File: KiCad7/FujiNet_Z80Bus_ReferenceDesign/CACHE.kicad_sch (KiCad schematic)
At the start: 4 parts, among them IC2 74590N, IC3 74590N

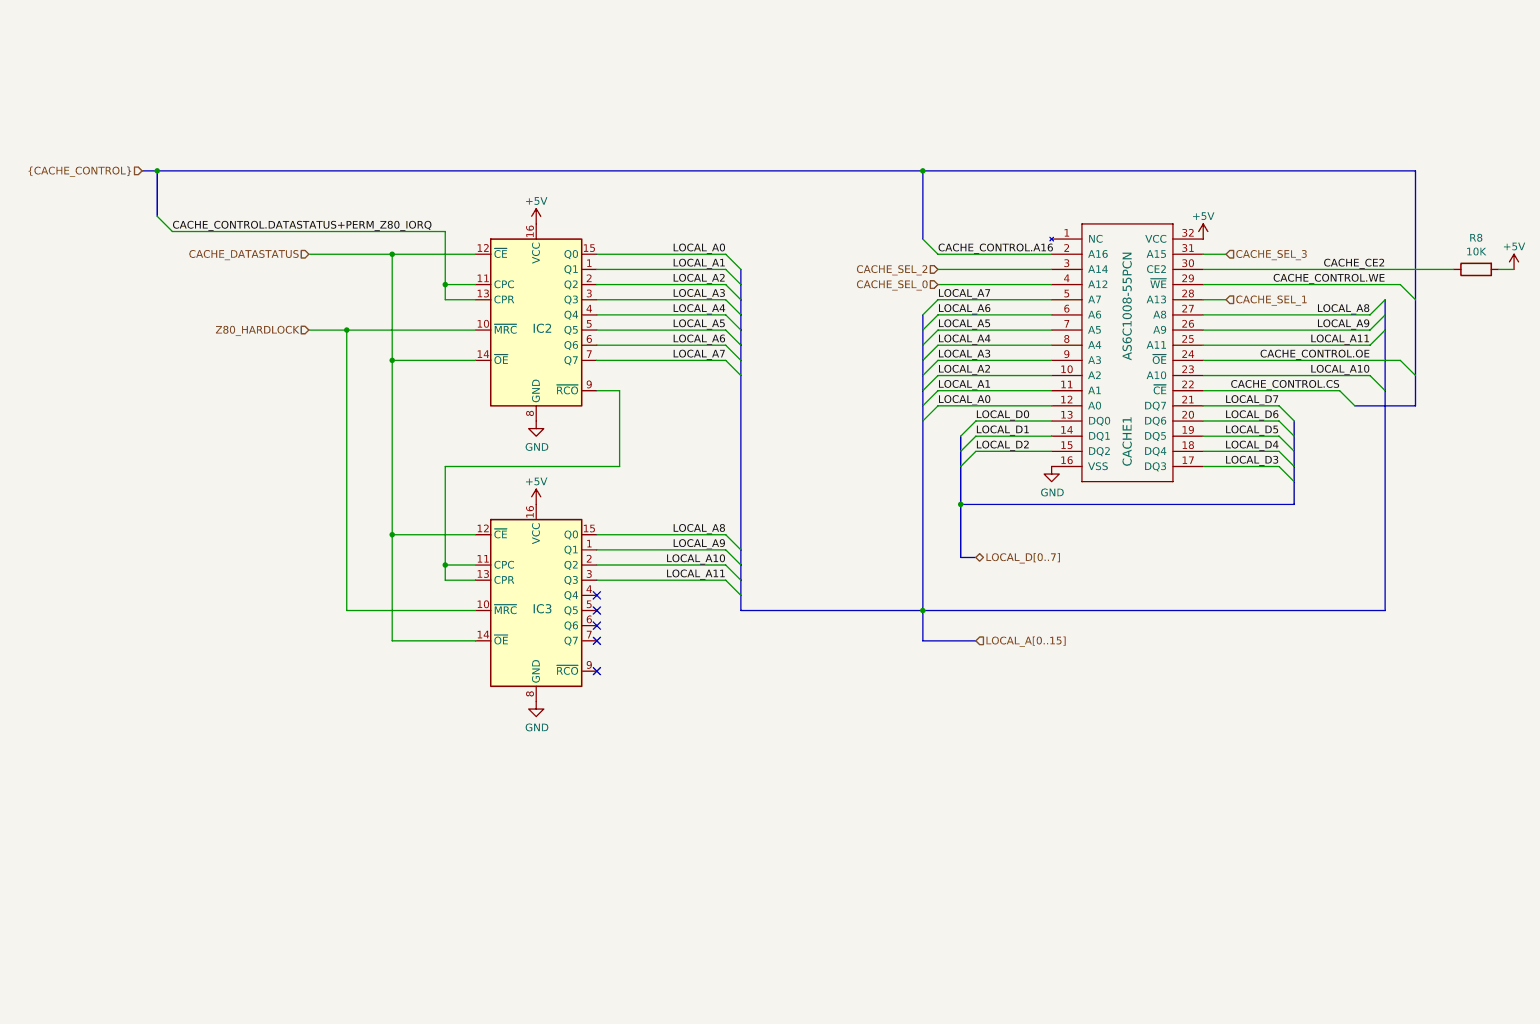
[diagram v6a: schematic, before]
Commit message: KiCad - Swapped out RIO and CACHE symbols
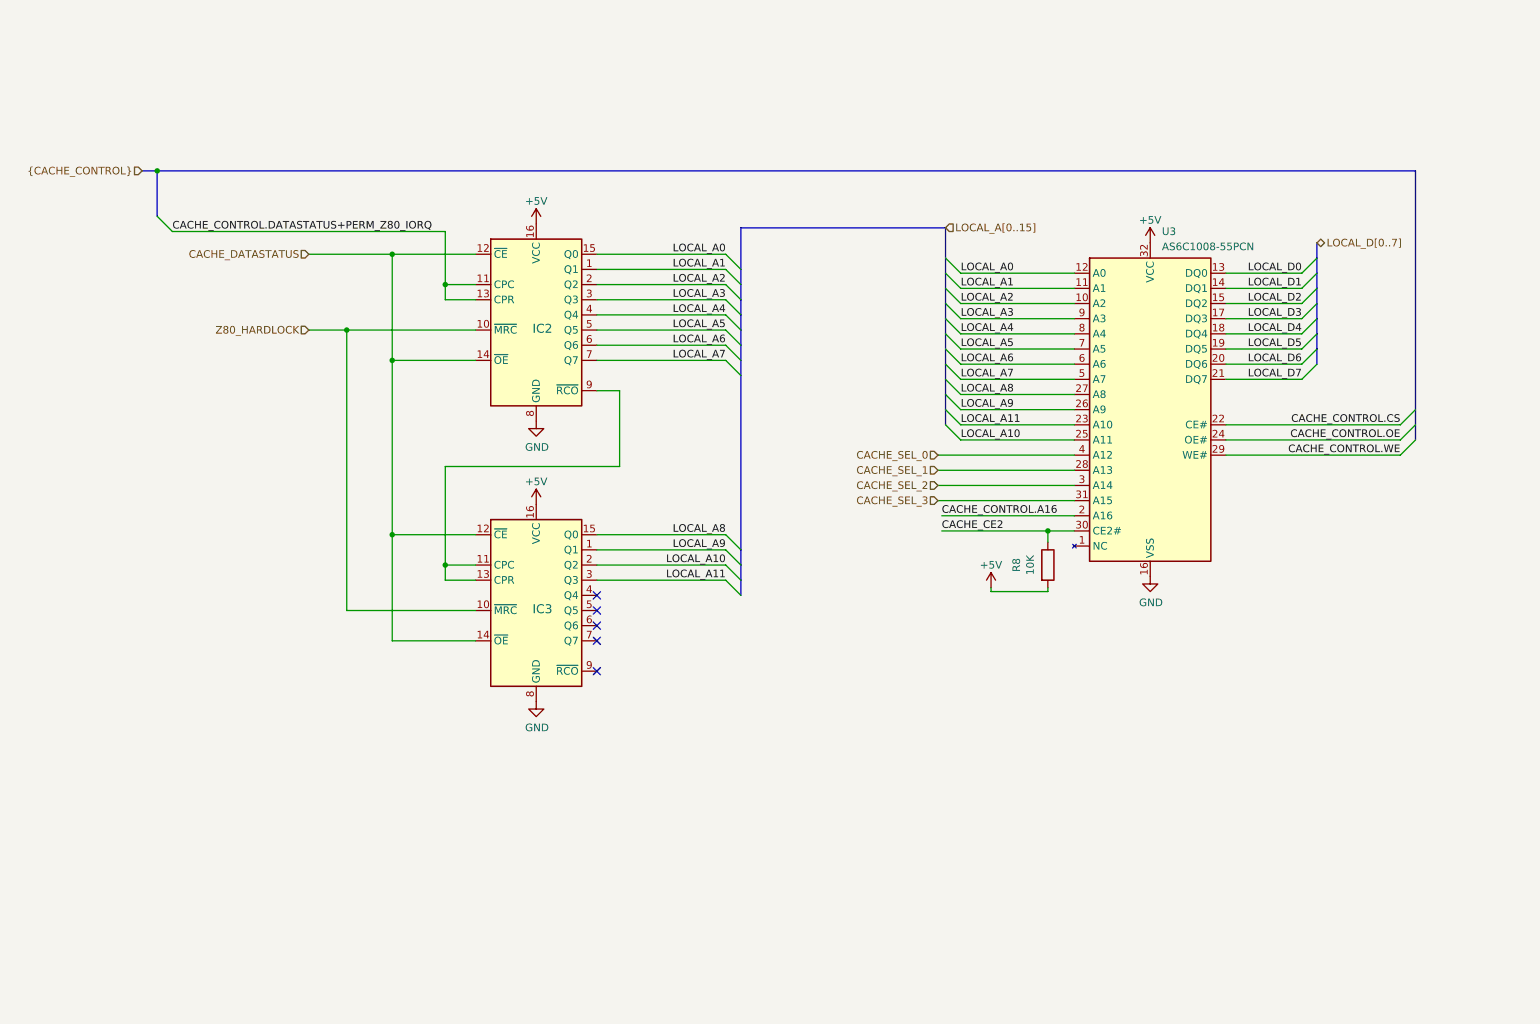
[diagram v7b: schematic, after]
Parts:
- removed CACHE1: AS6C1008-55PCN, Package_DIP:DIP-32_W15.24mm_Socket, symbol FujiNet_Z80Bus_Reference-rescue:AS6C1008-55PCN-Z80Decoder-eagle-import
- added U3: AS6C1008-55PCN, Package_DIP:DIP-32_W15.24mm, symbol FujiNet_Memory_RAM:AS6C1008-55PCN
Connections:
- net +5V: now also U3.32 (VCC)
- net CACHE_CE2: now also U3.30 (CE2#)
- net CACHE_CONTROL.A16: now also U3.2 (A16)
- net CACHE_CONTROL.CS: now also U3.22 (CE#)
- net CACHE_CONTROL.OE: now also U3.24 (OE#)
- net CACHE_CONTROL.WE: now also U3.29 (WE#)
- net CACHE_SEL_0: now also U3.4 (A12)
- net CACHE_SEL_1: now also U3.28 (A13)
- net CACHE_SEL_2: now also U3.3 (A14)
- net CACHE_SEL_3: now also U3.31 (A15)
- net GND: now also U3.16 (VSS)
- net LOCAL_A0: now also U3.12 (A0)
- net LOCAL_A1: now also U3.11 (A1)
- net LOCAL_A10: now also U3.25 (A11)
- net LOCAL_A11: now also U3.23 (A10)
- net LOCAL_A2: now also U3.10 (A2)
- net LOCAL_A3: now also U3.9 (A3)
- net LOCAL_A4: now also U3.8 (A4)
- net LOCAL_A5: now also U3.7 (A5)
- net LOCAL_A6: now also U3.6 (A6)
- net LOCAL_A7: now also U3.5 (A7)
- net LOCAL_A8: now also U3.27 (A8)
- net LOCAL_A9: now also U3.26 (A9)
- net LOCAL_D0: now also U3.13 (DQ0)
- net LOCAL_D1: now also U3.14 (DQ1)
- net LOCAL_D2: now also U3.15 (DQ2)
- net LOCAL_D3: now also U3.17 (DQ3)
- net LOCAL_D4: now also U3.18 (DQ4)
- net LOCAL_D5: now also U3.19 (DQ5)
- net LOCAL_D6: now also U3.20 (DQ6)
- net LOCAL_D7: now also U3.21 (DQ7)
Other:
- moved on the sheet: R8

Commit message: KiCAD PCB layout testing
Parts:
- IC2, IC3: value 74590N -> 74HC590N
- renumbered U3 to CACHE3
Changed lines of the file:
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@@
       (effects (font (size 1.4986 1.4986)) (justify left bottom))
     )
-    (property "Value" "74590N" (at 104.14 134.62 0)
+    (property "Value" "74HC590N" (at 104.14 134.62 0)
       (effects (font (size 1.4986 1.4986)) (justify left bottom) hide)
     )
@@
       (effects (font (size 1.4986 1.4986)) (justify left bottom))
     )
-    (property "Value" "74590N" (at 104.14 87.63 0)
+    (property "Value" "74HC590N" (at 104.14 87.63 0)
       (effects (font (size 1.4986 1.4986)) (justify left bottom) hide)
     )
@@
   (symbol (lib_id "FujiNet_Memory_RAM:AS6C1008-55PCN") (at 214.63 83.185 0) (unit 1)
     (in_bom yes) (on_board yes) (dnp no) (fields_autoplaced)
-    (property "Reference" "U3" (at 216.5859 53.34 0)
+    (property "Reference" "CACHE3" (at 216.5859 53.34 0)
       (effects (font (size 1.27 1.27)) (justify left))
     )
@@
       (project "FujiNet_Z80Bus_ReferenceDesign"
         (path "/532c0392-800e-45cc-8170-6d32f2390e83/00000000-0000-0000-0000-0000ae2cbb6b"
-          (reference "U3") (unit 1)
-        )
-      )
+          (reference "CACHE3") (unit 1)
+        )
+      )
